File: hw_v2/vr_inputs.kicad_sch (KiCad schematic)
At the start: 20 parts, among them U1 MAX9924UAUB_, U7 74LVC2G17

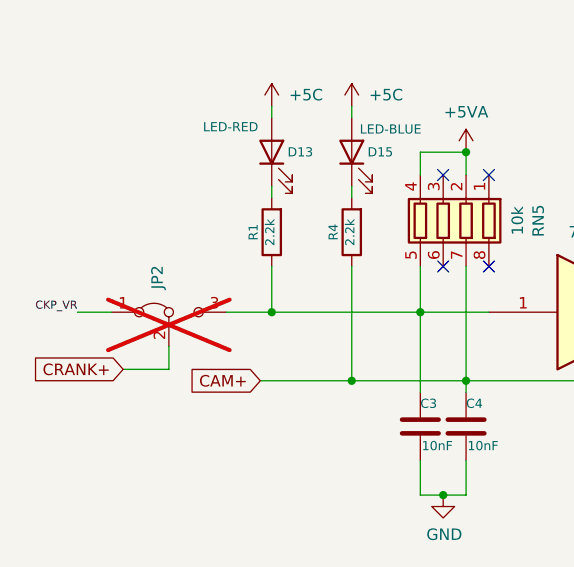
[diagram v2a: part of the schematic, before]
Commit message: update ADC oamp
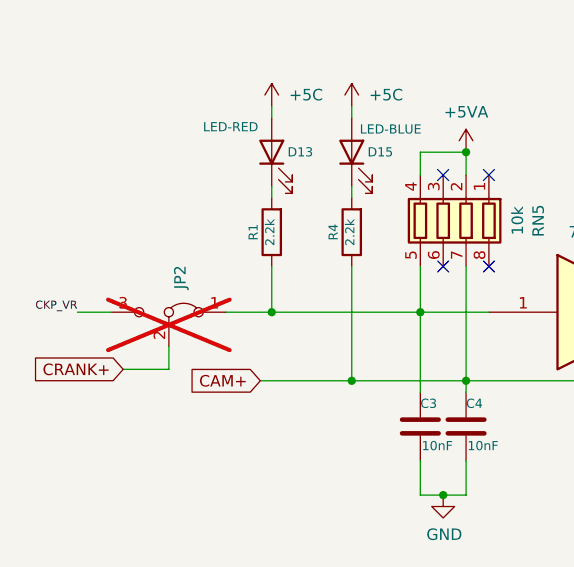
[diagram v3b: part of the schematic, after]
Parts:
- U7: LCSC (none) -> C80500
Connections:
- net CKP_VR: now also JP2.3 (B); no longer JP2.1 (A)
- net at C3.1, R1.1, RN5.5 (R4.2)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: now also JP2.1 (A); no longer JP2.3 (B)
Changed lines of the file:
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@@
+			)
+		)
+		(property "LCSC" "C80500"
+			(at 111.76 131.064 0)
+			(effects
+				(font
+					(size 1.27 1.27)
+				)
+				(hide yes)
 			)
 		)
@@
 		(lib_id "Jumper:Jumper_3_Bridged12")
 		(at 45.72 128.27 0)
+		(mirror y)
 		(unit 1)
 		(exclude_from_sim yes)
@@
 		(dnp yes)
 		(property "Reference" "JP2"
-			(at 44.45 125.73 90)
+			(at 46.99 125.73 90)
 			(effects
 				(font
@@
 		)
 		(property "Value" "Jumper_3_Bridged12"
-			(at 38.735 138.43 0)
+			(at 52.705 138.43 0)
 			(effects
 				(font
@@
 			)
 		)
+		(property "LCSC" "C80500"
+			(at 137.16 166.37 0)
+			(effects
+				(font
+					(size 1.27 1.27)
+				)
+				(hide yes)
+			)
+		)
 		(pin "3"
 		)
@@
 			(effects
 				(font
+					(size 1.27 1.27)
+				)
+				(hide yes)
+			)
+		)
+		(property "LCSC" "C80500"
+			(at 95.25 116.84 0)
+			(effects
+				(font
